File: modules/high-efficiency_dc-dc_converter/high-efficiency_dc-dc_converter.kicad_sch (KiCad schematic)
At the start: 12 parts

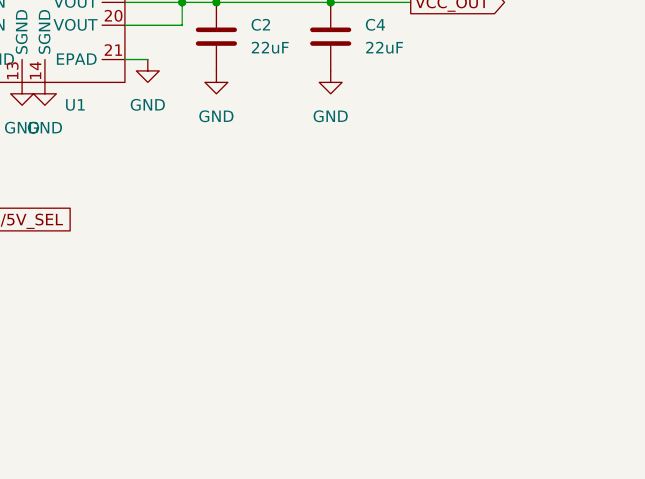
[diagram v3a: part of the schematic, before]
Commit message: add 2x11 module symbol and footprint and use for DC:DC module
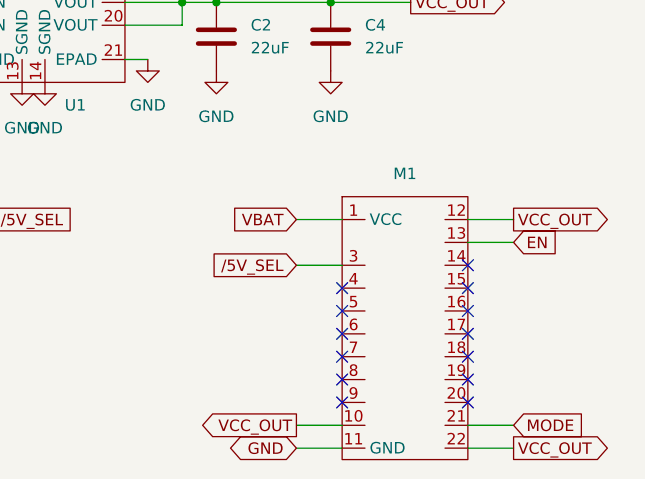
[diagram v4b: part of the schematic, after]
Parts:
- added M1: ~, MegaCastle:MegaCastle2x11Wide-Module-I13.2x22.25-KA0780C, symbol MegaCastle:MegaCastle2x11-Module
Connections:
- net +4V: now also M1.1 (VCC)
- net EN: now also M1.13
- net GND: now also M1.11 (GND)
- net MODE: now also M1.21
- net VCC_OUT: now also M1.10, M1.12, M1.22
- net /5V_SEL: now also M1.3
- no-connect marks 0 -> 13
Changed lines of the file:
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@@
   (junction (at 38.1 77.47) (diameter 0) (color 0 0 0 0)
   )
+  (no_connect (at 106.68 111.76))
+  (no_connect (at 106.68 109.22))
+  (no_connect (at 120.65 119.38))
+  (no_connect (at 120.65 111.76))
+  (no_connect (at 120.65 109.22))
+  (no_connect (at 120.65 106.68))
+  (no_connect (at 120.65 104.14))
+  (no_connect (at 106.68 116.84))
+  (no_connect (at 106.68 119.38))
+  (no_connect (at 106.68 106.68))
+  (no_connect (at 106.68 114.3))
+  (no_connect (at 120.65 114.3))
+  (no_connect (at 120.65 116.84))
   (wire (pts (xy 35.56 58.42) (xy 43.18 58.42))
     (stroke (width 0) (type default))
   )
+  (wire (pts (xy 101.6 104.14) (xy 106.68 104.14))
+    (stroke (width 0) (type default))
+  )
   (wire (pts (xy 82.55 77.47) (xy 88.9 77.47))
     (stroke (width 0) (type default))
@@
     (stroke (width 0) (type default))
   )
+  (wire (pts (xy 120.65 121.92) (xy 125.73 121.92))
+    (stroke (width 0) (type default))
+  )
+  (wire (pts (xy 120.65 99.06) (xy 125.73 99.06))
+    (stroke (width 0) (type default))
+  )
+  (wire (pts (xy 101.6 99.06) (xy 106.68 99.06))
+    (stroke (width 0) (type default))
+  )
   (wire (pts (xy 105.41 74.93) (xy 114.3 74.93))
     (stroke (width 0) (type default))
@@
     (stroke (width 0) (type default))
   )
+  (wire (pts (xy 120.65 124.46) (xy 125.73 124.46))
+    (stroke (width 0) (type default))
+  )
   (wire (pts (xy 115.57 48.26) (xy 115.57 72.39))
     (stroke (width 0) (type default))
@@
     (stroke (width 0) (type default))
   )
+  (wire (pts (xy 101.6 124.46) (xy 106.68 124.46))
+    (stroke (width 0) (type default))
+  )
   (wire (pts (xy 67.31 43.18) (xy 67.31 50.8))
     (stroke (width 0) (type default))
@@
     (stroke (width 0) (type default))
   )
+  (wire (pts (xy 101.6 121.92) (xy 106.68 121.92))
+    (stroke (width 0) (type default))
+  )
   (wire (pts (xy 82.55 81.28) (xy 85.09 81.28))
     (stroke (width 0) (type default))
@@
     (stroke (width 0) (type default))
   )
+  (wire (pts (xy 120.65 101.6) (xy 125.73 101.6))
+    (stroke (width 0) (type default))
+  )
+  (global_label "MODE" (shape input) (at 125.73 121.92 0) (fields_autoplaced)
+    (effects (font (size 1.27 1.27)) (justify left))
+    (property "Intersheetrefs" "${INTERSHEET_REFS}" (at 133.9161 121.92 0)
+      (effects (font (size 1.27 1.27)) (justify left) hide)
+    )
+  )
   (global_label "{slash}5V_SEL" (shape input) (at 67.31 99.06 0) (fields_autoplaced)
     (effects (font (size 1.27 1.27)) (justify left))
@@
     )
   )
+  (global_label "EN" (shape input) (at 125.73 101.6 0) (fields_autoplaced)
+    (effects (font (size 1.27 1.27)) (justify left))
+    (property "Intersheetrefs" "${INTERSHEET_REFS}" (at 131.1947 101.6 0)
+      (effects (font (size 1.27 1.27)) (justify left) hide)
+    )
+  )
   (global_label "GND" (shape bidirectional) (at 35.56 64.77 180) (fields_autoplaced)
     (effects (font (size 1.27 1.27)) (justify right))
@@
     )
   )
+  (global_label "VBAT" (shape input) (at 101.6 99.06 180) (fields_autoplaced)
+    (effects (font (size 1.27 1.27)) (justify right))
+    (property "Intersheetrefs" "${INTERSHEET_REFS}" (at 94.2 99.06 0)
+      (effects (font (size 1.27 1.27)) (justify right) hide)
+    )
+  )
+  (global_label "VCC_OUT" (shape output) (at 101.6 121.92 180) (fields_autoplaced)
+    (effects (font (size 1.27 1.27)) (justify right))
+    (property "Intersheetrefs" "${INTERSHEET_REFS}" (at 90.39 121.92 0)
+      (effects (font (size 1.27 1.27)) (justify right) hide)
+    )
+  )
   (global_label "VCC_OUT" (shape output) (at 114.3 74.93 0) (fields_autoplaced)
     (effects (font (size 1.27 1.27)) (justify left))
@@
     )
   )
+  (global_label "VCC_OUT" (shape output) (at 125.73 99.06 0) (fields_autoplaced)
+    (effects (font (size 1.27 1.27)) (justify left))
+    (property "Intersheetrefs" "${INTERSHEET_REFS}" (at 136.94 99.06 0)
+      (effects (font (size 1.27 1.27)) (justify left) hide)
+    )
+  )
+  (global_label "{slash}5V_SEL" (shape input) (at 101.6 104.14 180) (fields_autoplaced)
+    (effects (font (size 1.27 1.27)) (justify right))
+    (property "Intersheetrefs" "${INTERSHEET_REFS}" (at 90.632 104.14 0)
+      (effects (font (size 1.27 1.27)) (justify right) hide)
+    )
+  )
   (global_label "EN" (shape input) (at 52.07 62.23 180) (fields_autoplaced)
     (effects (font (size 1.27 1.27)) (justify right))
     (property "Intersheetrefs" "${INTERSHEET_REFS}" (at 46.6053 62.23 0)
+      (effects (font (size 1.27 1.27)) (justify right) hide)
+    )
+  )
+  (global_label "VCC_OUT" (shape output) (at 125.73 124.46 0) (fields_autoplaced)
+    (effects (font (size 1.27 1.27)) (justify left))
+    (property "Intersheetrefs" "${INTERSHEET_REFS}" (at 136.94 124.46 0)
+      (effects (font (size 1.27 1.27)) (justify left) hide)
+    )
+  )
+  (global_label "GND" (shape bidirectional) (at 101.6 124.46 180) (fields_autoplaced)
+    (effects (font (size 1.27 1.27)) (justify right))
+    (property "Intersheetrefs" "${INTERSHEET_REFS}" (at 93.633 124.46 0)
       (effects (font (size 1.27 1.27)) (justify right) hide)
     )
@@
         )
       )
+    )
+  )
+  (symbol (lib_id "MegaCastle:MegaCastle2x11-Module") (at 113.03 110.49 0) (unit 1)
+    (in_bom yes) (on_board yes) (dnp no) (fields_autoplaced)
+    (property "Reference" "M1" (at 113.665 93.98 0)
+      (effects (font (size 1.27 1.27)))
+    )
+    (property "Value" "~" (at 113.03 105.41 0)
+      (effects (font (size 1.27 1.27)))
+    )
+    (property "Footprint" "MegaCastle:MegaCastle2x11Wide-Module-I13.2x22.25-KA0780C" (at 113.03 105.41 0)
+      (effects (font (size 1.27 1.27)) hide)
+    )
+    (property "Datasheet" "" (at 113.03 105.41 0)
+      (effects (font (size 1.27 1.27)) hide)
+    )
+    (pin "5")
+    (pin "9")
+    (pin "4")
+    (pin "7")
+    (pin "6")
+    (pin "20")
+    (pin "13")
+    (pin "19")
+    (pin "12")
+    (pin "11")
+    (pin "10")
+    (pin "22")
+    (pin "18")
+    (pin "16")
+    (pin "21")
+    (pin "17")
+    (pin "3")
+    (pin "14")
+    (pin "15")
+    (pin "1")
+    (pin "8")
+    (instances
+      (project "high-efficiency_dc-dc_converter"
+        (path "/7f4a2112-cc8e-483f-9ea5-76225b466e70"
+          (reference "M1") (unit 1)
+        )
+      )

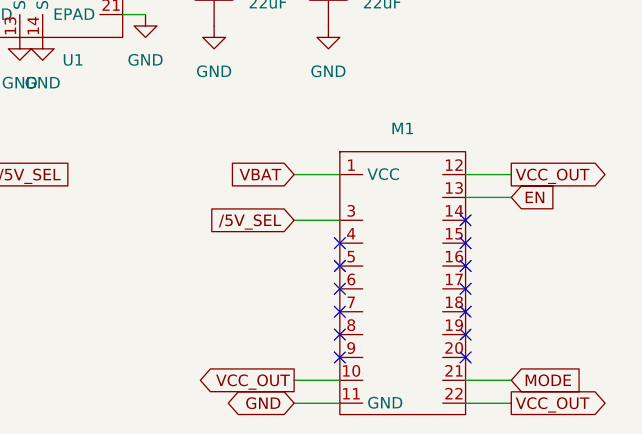
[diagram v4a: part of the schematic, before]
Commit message: rearrange pins etc to keep to 2-layer for DC:DC module
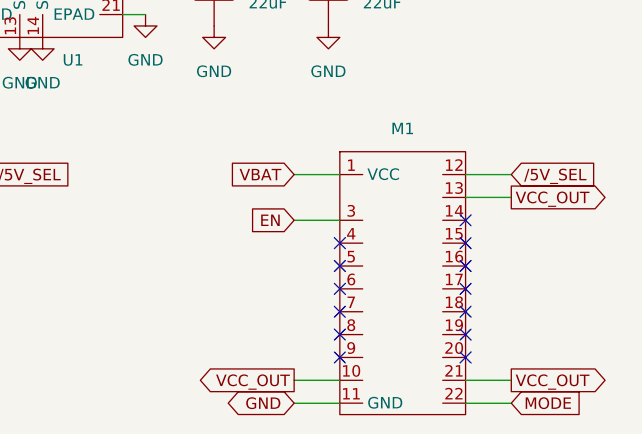
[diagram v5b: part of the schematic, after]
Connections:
- net EN: now also M1.3; no longer M1.13
- net MODE: now also M1.22; no longer M1.21
- net VCC_OUT: now also M1.13, M1.21; no longer M1.12, M1.22
- net /5V_SEL: now also M1.12; no longer M1.3
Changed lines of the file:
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@@
     (stroke (width 0) (type default))
   )
-  (global_label "MODE" (shape input) (at 125.73 121.92 0) (fields_autoplaced)
-    (effects (font (size 1.27 1.27)) (justify left))
-    (property "Intersheetrefs" "${INTERSHEET_REFS}" (at 133.9161 121.92 0)
-      (effects (font (size 1.27 1.27)) (justify left) hide)
+  (global_label "EN" (shape input) (at 101.6 104.14 180) (fields_autoplaced)
+    (effects (font (size 1.27 1.27)) (justify right))
+    (property "Intersheetrefs" "${INTERSHEET_REFS}" (at 96.1353 104.14 0)
+      (effects (font (size 1.27 1.27)) (justify right) hide)
     )
   )
@@
     )
   )
+  (global_label "MODE" (shape input) (at 125.73 124.46 0) (fields_autoplaced)
+    (effects (font (size 1.27 1.27)) (justify left))
+    (property "Intersheetrefs" "${INTERSHEET_REFS}" (at 133.9161 124.46 0)
+      (effects (font (size 1.27 1.27)) (justify left) hide)
+    )
+  )
   (global_label "VBAT" (shape input) (at 35.56 58.42 180) (fields_autoplaced)
     (effects (font (size 1.27 1.27)) (justify right))
@@
     )
   )
-  (global_label "EN" (shape input) (at 125.73 101.6 0) (fields_autoplaced)
+  (global_label "VCC_OUT" (shape output) (at 125.73 101.6 0) (fields_autoplaced)
     (effects (font (size 1.27 1.27)) (justify left))
-    (property "Intersheetrefs" "${INTERSHEET_REFS}" (at 131.1947 101.6 0)
+    (property "Intersheetrefs" "${INTERSHEET_REFS}" (at 136.94 101.6 0)
       (effects (font (size 1.27 1.27)) (justify left) hide)
     )
@@
     )
   )
+  (global_label "VCC_OUT" (shape output) (at 125.73 121.92 0) (fields_autoplaced)
+    (effects (font (size 1.27 1.27)) (justify left))
+    (property "Intersheetrefs" "${INTERSHEET_REFS}" (at 136.94 121.92 0)
+      (effects (font (size 1.27 1.27)) (justify left) hide)
+    )
+  )
   (global_label "VCC_OUT" (shape output) (at 114.3 74.93 0) (fields_autoplaced)
     (effects (font (size 1.27 1.27)) (justify left))
     (property "Intersheetrefs" "${INTERSHEET_REFS}" (at 125.51 74.93 0)
       (effects (font (size 1.27 1.27)) (justify left) hide)
-    )
-  )
-  (global_label "VCC_OUT" (shape output) (at 125.73 99.06 0) (fields_autoplaced)
-    (effects (font (size 1.27 1.27)) (justify left))
-    (property "Intersheetrefs" "${INTERSHEET_REFS}" (at 136.94 99.06 0)
-      (effects (font (size 1.27 1.27)) (justify left) hide)
-    )
-  )
-  (global_label "{slash}5V_SEL" (shape input) (at 101.6 104.14 180) (fields_autoplaced)
-    (effects (font (size 1.27 1.27)) (justify right))
-    (property "Intersheetrefs" "${INTERSHEET_REFS}" (at 90.632 104.14 0)
-      (effects (font (size 1.27 1.27)) (justify right) hide)
     )
   )
@@
     )
   )
-  (global_label "VCC_OUT" (shape output) (at 125.73 124.46 0) (fields_autoplaced)
+  (global_label "{slash}5V_SEL" (shape input) (at 125.73 99.06 0) (fields_autoplaced)
     (effects (font (size 1.27 1.27)) (justify left))
-    (property "Intersheetrefs" "${INTERSHEET_REFS}" (at 136.94 124.46 0)
+    (property "Intersheetrefs" "${INTERSHEET_REFS}" (at 136.698 99.06 0)
       (effects (font (size 1.27 1.27)) (justify left) hide)
     )
